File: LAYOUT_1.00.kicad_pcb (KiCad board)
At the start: 2 copper layers, 212.1 x 207 mm, 122 parts, among them K1 CONN_3, SW1 DPST, SW10 DPST, SW11 DPST, SW12 DPST, SW13 DPST, SW14 DPST, SW15 DPST, SW16 DPST, SW2 DPST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

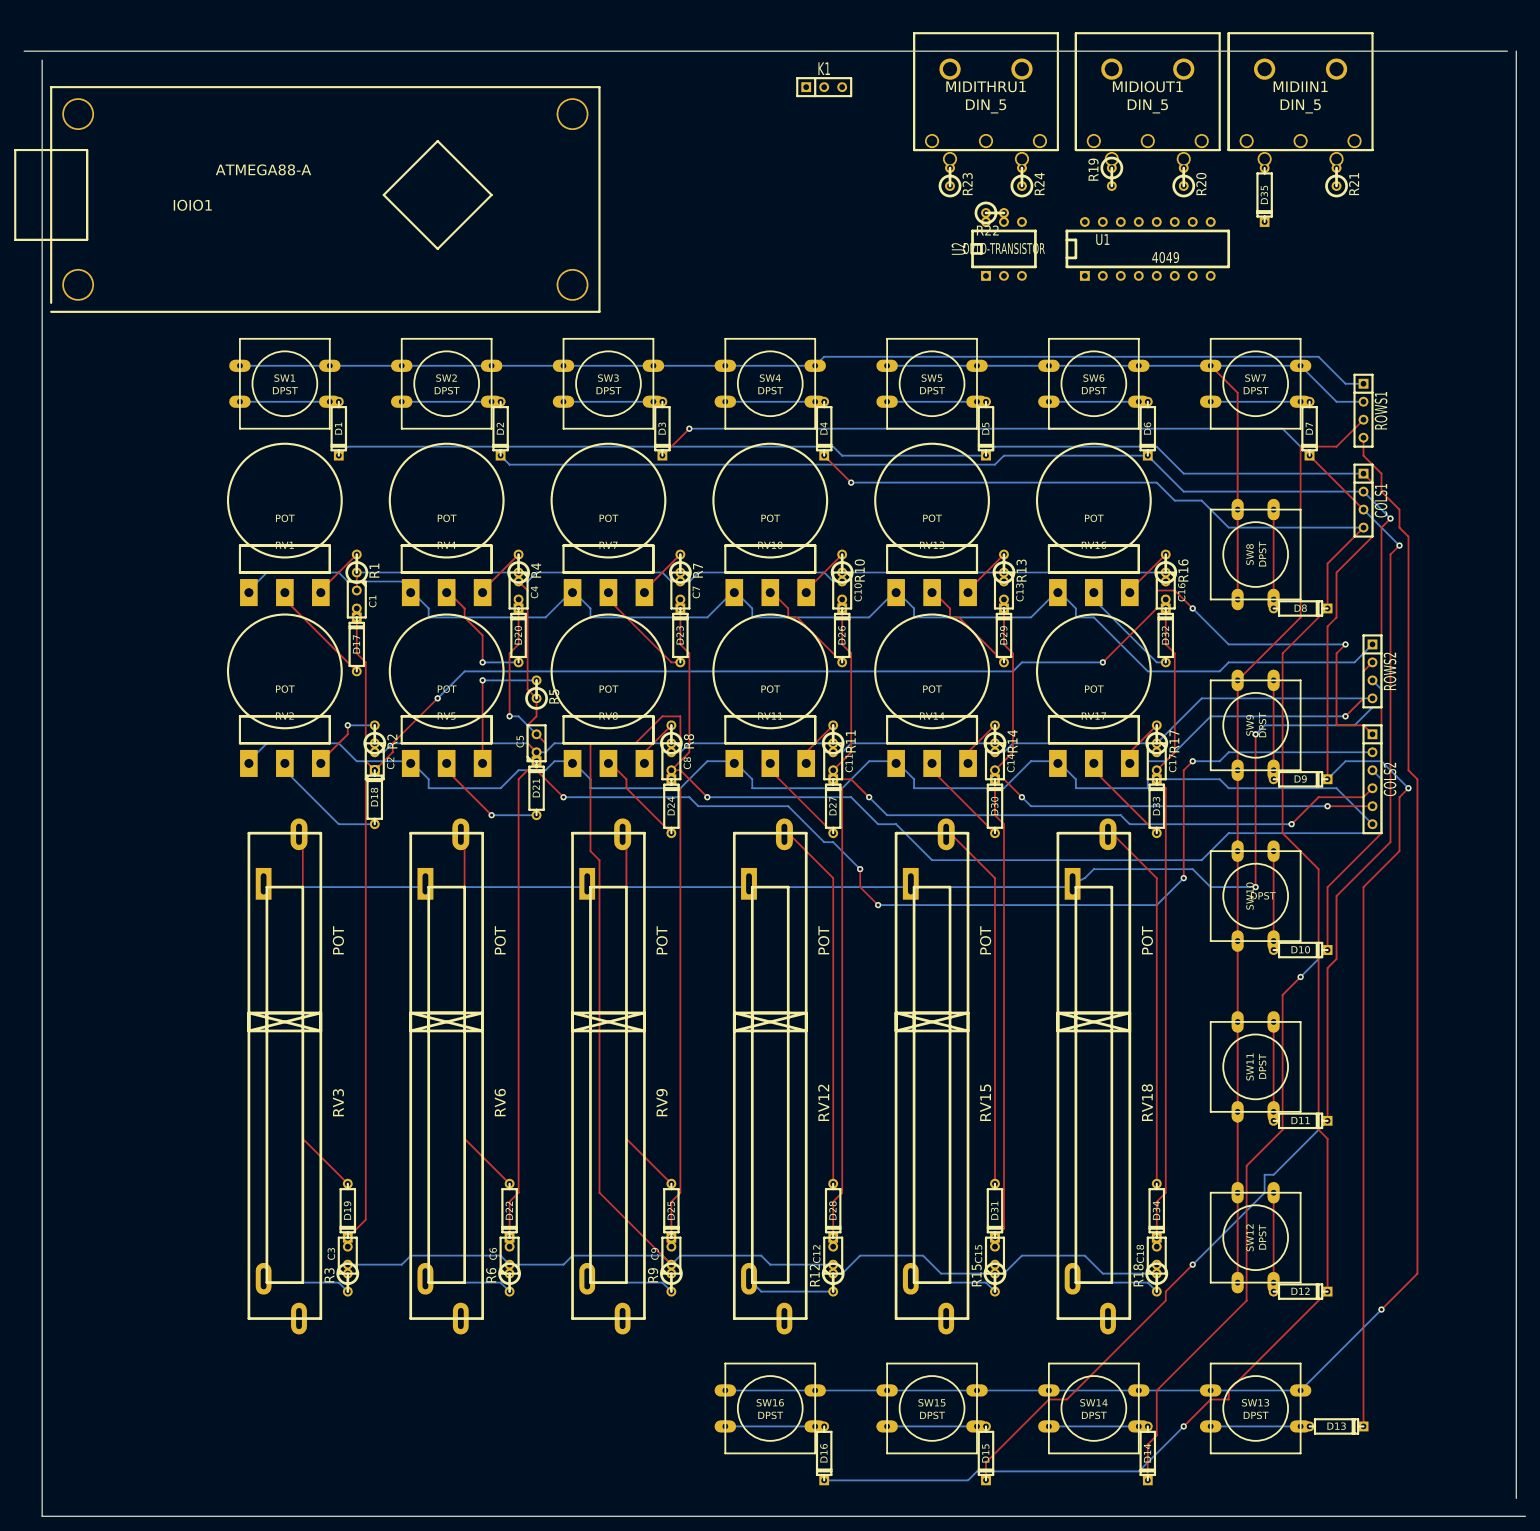
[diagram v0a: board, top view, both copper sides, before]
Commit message: Layout complete with parts
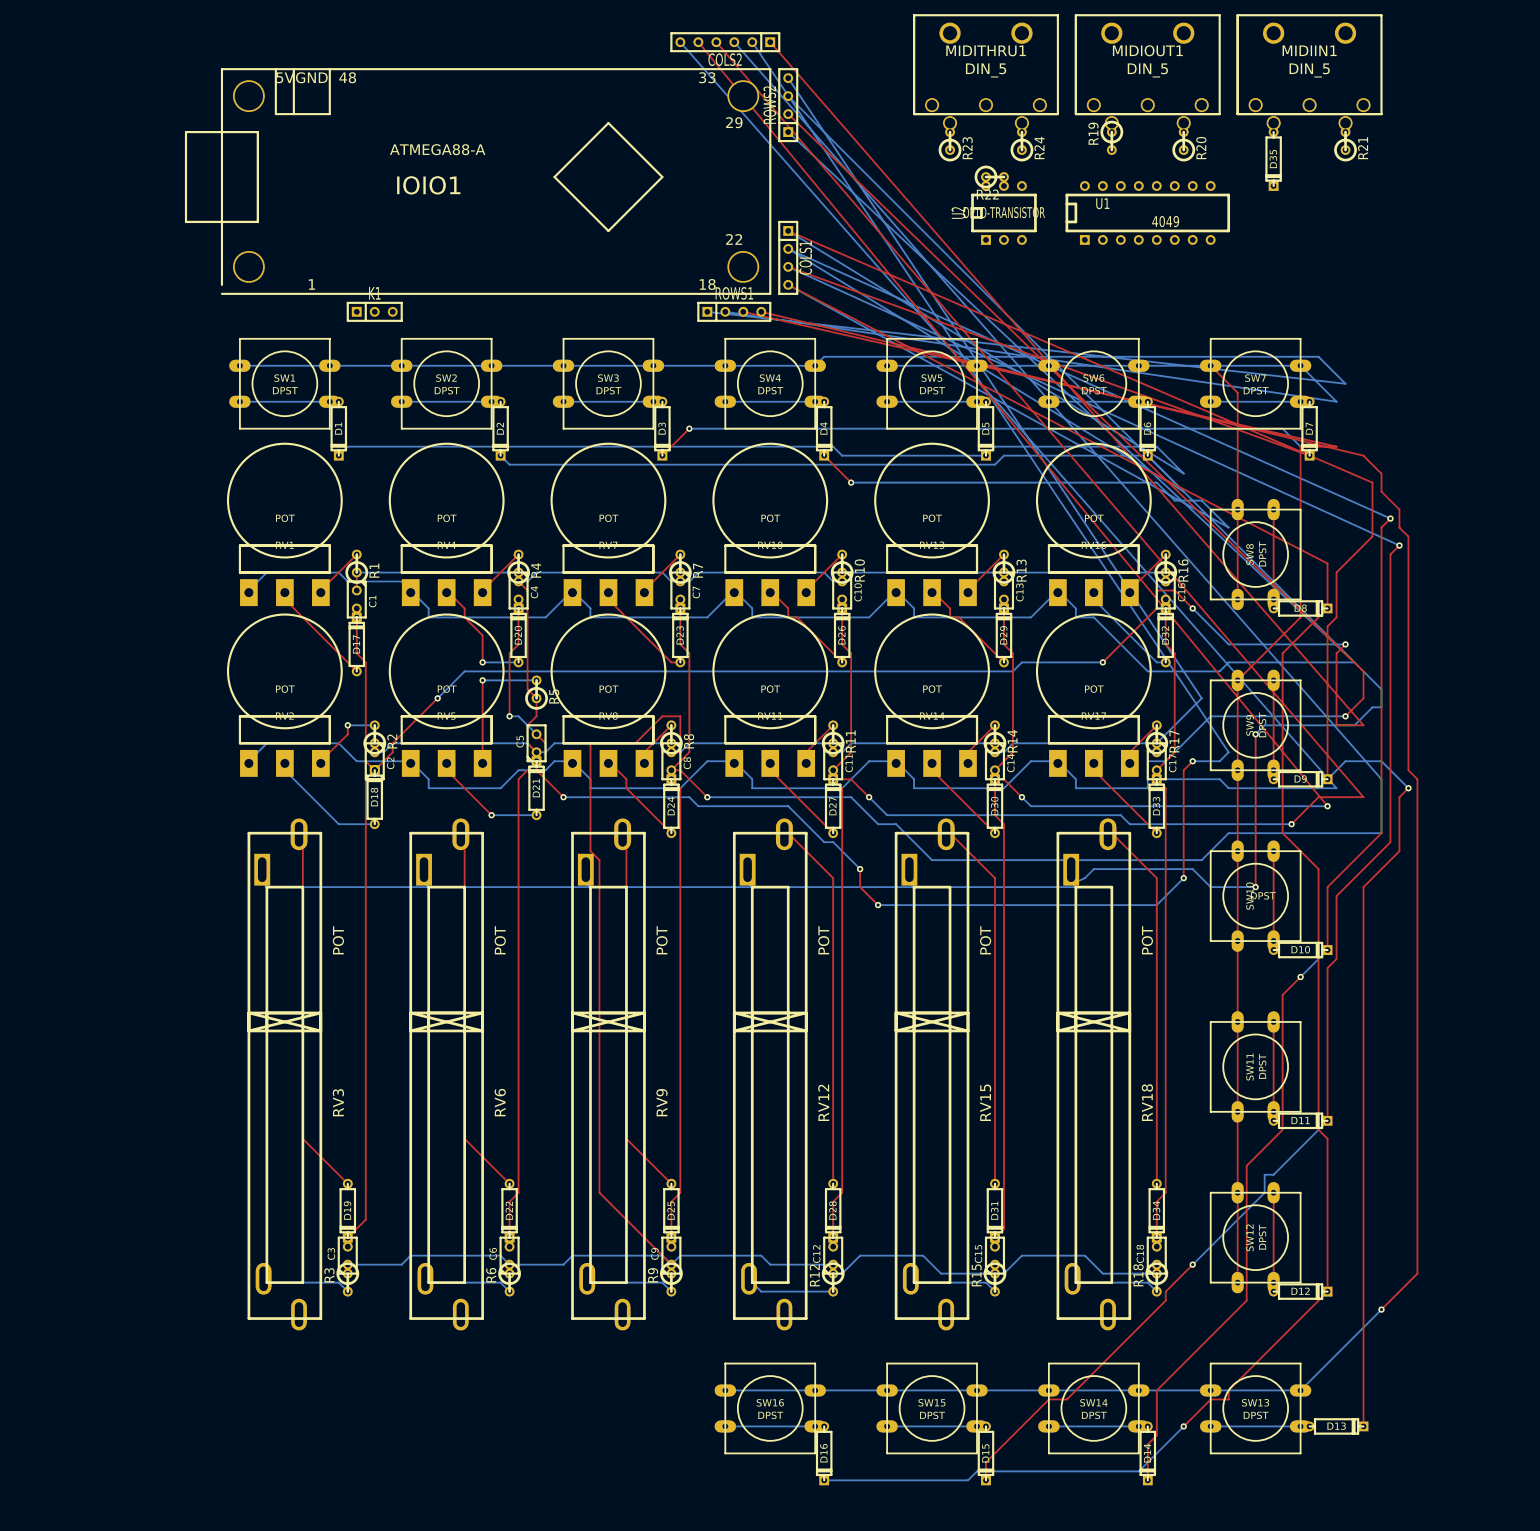
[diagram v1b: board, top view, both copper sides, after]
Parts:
- moved COLS2 138.6 mm to (86.4, 41.9), turned to 180 degrees
- moved ROWS2 115.0 mm to (95.2, 50.8), turned to 90 degrees
- moved ROWS1 90.0 mm to (87.6, 80.0), turned to 0 degrees
- moved COLS1 88.2 mm to (95.2, 72.4)
- moved K1 71.0 mm to (36.8, 80.0)
- moved IOIO1 24.3 mm to (15.2, 77.5)
- moved MIDIIN1 5.24 mm to (168.9, 50.8)
- moved D35 5.24 mm to (163.8, 58.4)
- moved R21 5.24 mm to (174.0, 55.9)
- moved MIDIOUT1 5.08 mm to (146.1, 50.8)
- moved MIDITHRU1 5.08 mm to (123.2, 50.8)
- moved R22 5.08 mm to (124.5, 61.0)
- moved R19 5.08 mm to (141.0, 55.9)
- moved R20 5.08 mm to (151.1, 55.9)
- moved R23 5.08 mm to (118.1, 55.9)
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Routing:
- net /c3: track 271.1 -> 426.4 mm
- net /col4: track 175.0 -> 313.7 mm
- net /col3: track 210.7 -> 347.4 mm
- net /col5: track 149.0 -> 282.5 mm
- net /col6: track 127.2 -> 260.4 mm
- net /c4: track 278.6 -> 409.2 mm
- net /c1: track 301.1 -> 429.4 mm
- net /c2: track 280.6 -> 408.6 mm
- net /col1: track 263.4 -> 389.5 mm
- net /row3: track 193.7 -> 310.5 mm
- net /row2: track 193.9 -> 305.3 mm
- net /row1: track 186.8 -> 292.8 mm
- net /col2: track 244.3 -> 344.8 mm
- net /a1: track 160.9 -> 249.1 mm
- net /a4: track 225.9 -> 310.8 mm
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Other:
- board outline removed
